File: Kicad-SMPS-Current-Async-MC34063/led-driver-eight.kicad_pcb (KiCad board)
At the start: 2 copper layers, 70 x 80 mm, 160 parts, among them J1 Input 12V-30V, J2 Output, J3 Conn_01x01, U1 MC34063, U2 LM321

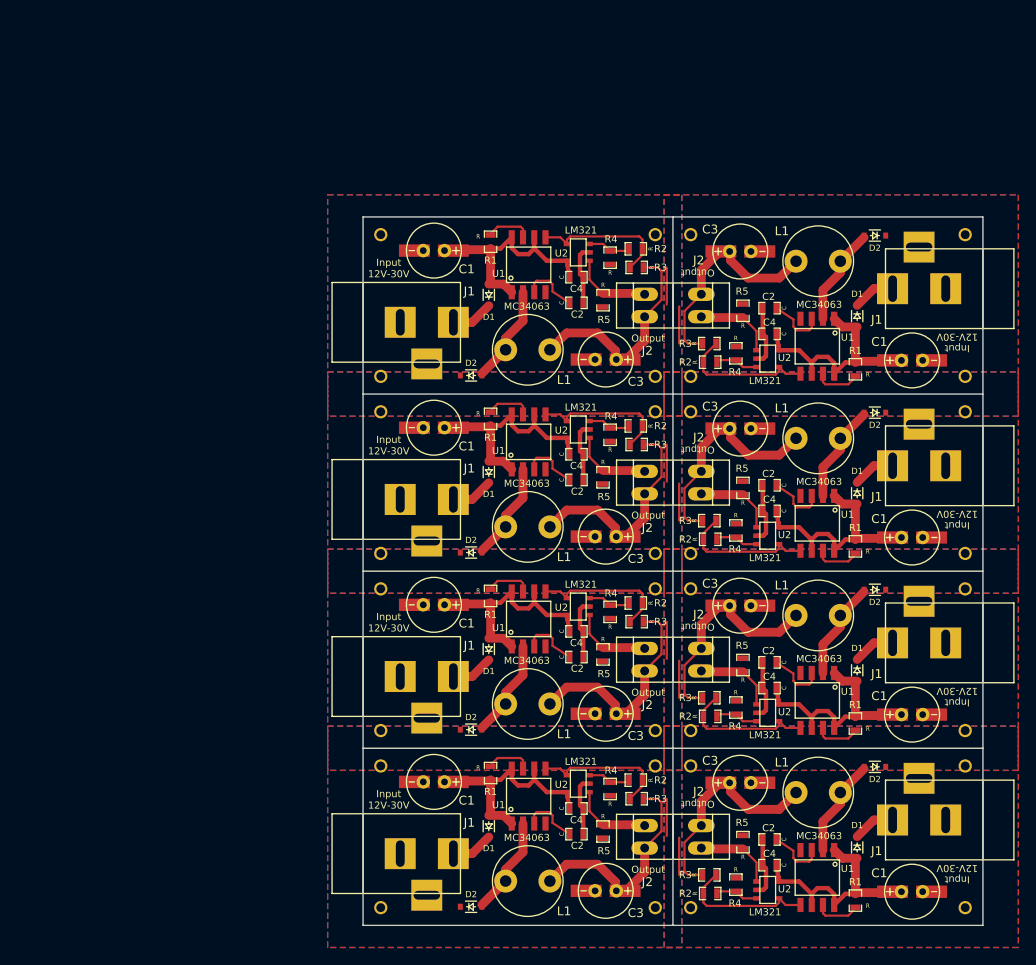
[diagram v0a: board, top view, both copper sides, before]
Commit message: Fix problem with current limiting resistor and also silk screen of diodes.
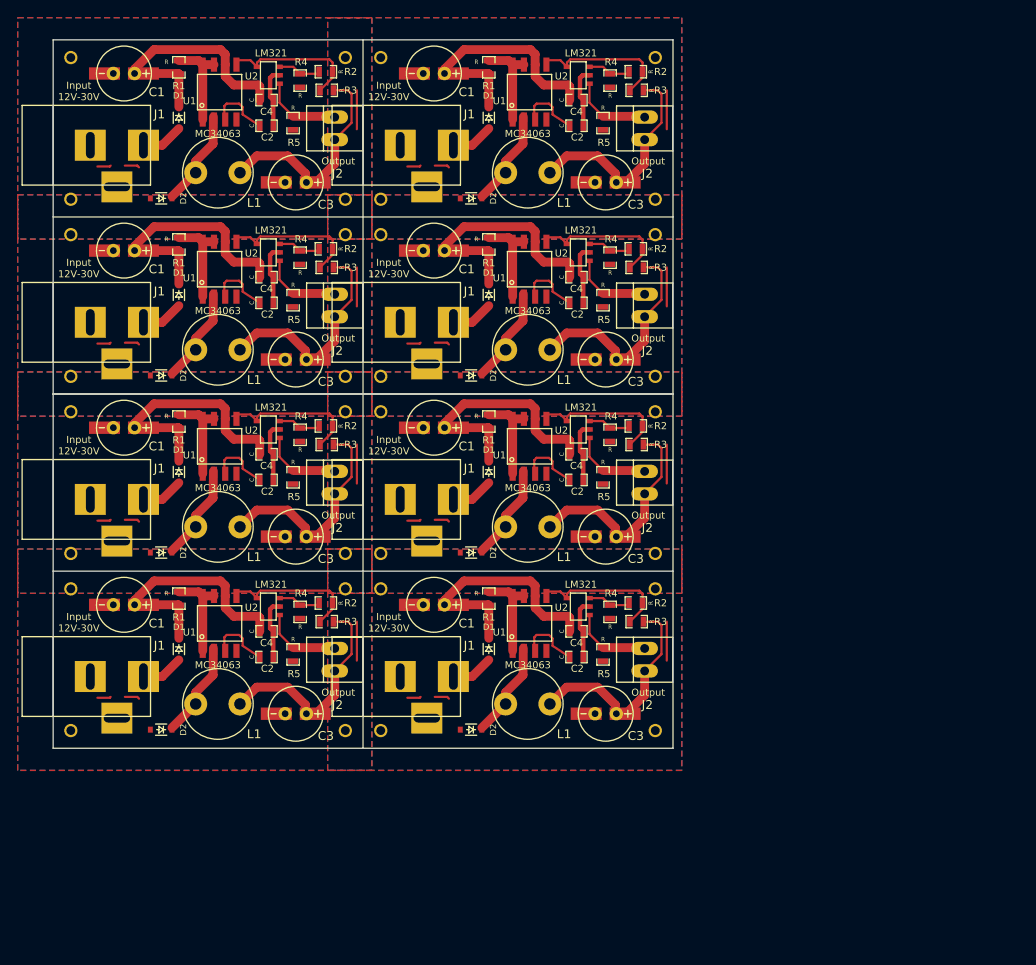
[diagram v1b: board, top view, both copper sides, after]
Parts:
- removed the C1 at (186.0, 83.7)
- removed the C1 at (186.0, 103.7)
- removed the C1 at (186.0, 143.7)
- removed the C1 at (186.0, 123.7)
- removed the C1 at (132.0, 131.3)
- removed the C2 at (169.9, 77.8)
- removed the C2 at (169.9, 97.8)
- removed the C2 at (169.9, 137.8)
- removed the C2 at (169.9, 117.8)
- removed the C2 at (148.1, 137.2)
- removed the C3 at (166.6, 71.4)
- removed the C3 at (166.6, 91.4)
- removed the C3 at (166.6, 131.4)
- removed the C3 at (166.6, 111.4)
- removed the C3 at (151.4, 143.6)
- removed the C4 at (169.9, 80.7)
- removed the C4 at (169.9, 100.7)
- removed the C4 at (169.9, 140.7)
- removed the C4 at (169.9, 120.7)
- removed the C4 at (148.1, 134.3)
- removed the D1 at (179.8, 78.7)
- removed the D1 at (179.8, 98.7)
- removed the D1 at (179.8, 138.7)
- removed the D1 at (179.8, 118.7)
- removed the D1 at (138.2, 136.3)
- removed the D2 at (181.8, 69.6)
- removed the D2 at (181.8, 89.6)
- removed the D2 at (181.8, 129.6)
- removed the D2 at (181.8, 109.6)
- removed the D2 at (136.2, 145.4)
- removed the J1 at (190.0, 75.6)
- removed the J1 at (190.0, 95.6)
- removed the J1 at (190.0, 135.6)
- removed the J1 at (190.0, 115.6)
- removed the J1 at (128.0, 139.4)
- removed the J2 at (162.2, 77.5)
- removed the J2 at (162.2, 97.5)
- removed the J2 at (162.2, 137.5)
- removed the J2 at (162.2, 117.5)
- removed the J2 at (155.8, 137.5)
- removed the J3 at (161.0, 85.5)
- removed the J3 at (192.0, 145.5)
- removed the J3 at (192.0, 129.5)
- removed the J3 at (161.0, 129.5)
- removed the J3 at (161.0, 109.5)
- removed the J3 at (192.0, 109.5)
- removed the J3 at (192.0, 125.5)
- removed the J3 at (161.0, 125.5)
- removed the J3 at (192.0, 85.5)
- removed the J3 at (157.0, 145.5)
- removed the J3 at (192.0, 69.5)
- removed the J3 at (126.0, 145.5)
- removed the J3 at (126.0, 129.5)
- removed the J3 at (157.0, 129.5)
- removed the J3 at (161.0, 69.5)
- removed the J3 at (161.0, 89.5)
- removed the J3 at (192.0, 89.5)
- removed the J3 at (192.0, 105.5)
- removed the J3 at (161.0, 105.5)
- removed the J3 at (161.0, 145.5)
- removed the L1 at (177.9, 72.5)
- removed the L1 at (177.9, 92.5)
- removed the L1 at (177.9, 132.5)
- removed the L1 at (177.9, 112.5)
- removed the L1 at (140.1, 142.5)
- removed the R1 at (179.6, 84.7)
- removed the R1 at (179.6, 104.7)
- removed the R1 at (179.6, 144.7)
- removed the R1 at (179.6, 124.7)
- removed the R1 at (138.4, 90.3)
- removed the R1 at (138.4, 70.3)
- removed the R1 at (138.4, 130.3)
- removed the R2 at (163.2, 83.9)
- removed the R2 at (163.2, 103.9)
- removed the R2 at (163.2, 143.9)
- removed the R2 at (163.2, 123.9)
- removed the R2 at (154.8, 131.1)
- removed the R3 at (163.1, 81.8)
- removed the R3 at (163.1, 101.8)
- removed the R3 at (163.1, 141.8)
- removed the R3 at (163.1, 121.8)
- removed the R3 at (154.9, 133.2)
- removed the R4 at (166.1, 82.9)
- removed the R4 at (166.1, 102.9)
- removed the R4 at (166.1, 142.9)
- removed the R4 at (166.1, 122.9)
- removed the R4 at (151.9, 132.1)
- removed the R5 at (166.9, 78.1)
- removed the R5 at (166.9, 98.1)
- removed the R5 at (166.9, 138.1)
- removed the R5 at (166.9, 118.1)
- removed the R5 at (151.1, 136.9)
- removed the U1 at (175.3, 82.1)
- removed the U1 at (175.3, 102.1)
- removed the U1 at (175.3, 142.1)
- removed the U1 at (175.3, 122.1)
- removed the U1 at (142.7, 92.9)
- removed the U1 at (142.7, 72.9)
- removed the U1 at (142.7, 132.9)
- removed the U2 at (169.7, 83.5)
- removed the U2 at (169.7, 103.5)
- removed the U2 at (169.7, 143.5)
- removed the U2 at (169.7, 123.5)
- removed the U2 at (148.3, 131.5)
- added C1: CP, smps-current-source:RADIAL_TABBED_2.5mm_6.3mm, F.Cu at (132.0, 51.3)
- added C1: CP, smps-current-source:RADIAL_TABBED_2.5mm_6.3mm, F.Cu at (97.0, 51.3)
- added C1: CP, smps-current-source:RADIAL_TABBED_2.5mm_6.3mm, F.Cu at (97.0, 71.3)
- added C1: CP, smps-current-source:RADIAL_TABBED_2.5mm_6.3mm, F.Cu at (97.0, 111.3)
- added C1: CP, smps-current-source:RADIAL_TABBED_2.5mm_6.3mm, F.Cu at (97.0, 91.3)
- added C2: C, smps-current-source:SM0603_Capa, F.Cu at (148.1, 57.2)
- added C2: C, smps-current-source:SM0603_Capa, F.Cu at (113.1, 57.2)
- added C2: C, smps-current-source:SM0603_Capa, F.Cu at (113.1, 77.2)
- added C2: C, smps-current-source:SM0603_Capa, F.Cu at (113.1, 117.2)
- added C2: C, smps-current-source:SM0603_Capa, F.Cu at (113.1, 97.2)
- added C3: CP, smps-current-source:RADIAL_TABBED_2.5mm_6.3mm, F.Cu at (151.4, 63.6)
- added C3: CP, smps-current-source:RADIAL_TABBED_2.5mm_6.3mm, F.Cu at (116.4, 63.6)
- added C3: CP, smps-current-source:RADIAL_TABBED_2.5mm_6.3mm, F.Cu at (116.4, 83.6)
- added C3: CP, smps-current-source:RADIAL_TABBED_2.5mm_6.3mm, F.Cu at (116.4, 123.6)
- added C3: CP, smps-current-source:RADIAL_TABBED_2.5mm_6.3mm, F.Cu at (116.4, 103.6)
- added C4: C, smps-current-source:SM0603_Capa, F.Cu at (148.1, 54.3)
- added C4: C, smps-current-source:SM0603_Capa, F.Cu at (113.1, 54.3)
- added C4: C, smps-current-source:SM0603_Capa, F.Cu at (113.1, 74.3)
- added C4: C, smps-current-source:SM0603_Capa, F.Cu at (113.1, 114.3)
- added C4: C, smps-current-source:SM0603_Capa, F.Cu at (113.1, 94.3)
- added D1: CUS15S30, smps-current-source:SOD-323, F.Cu at (138.2, 56.3)
- added D1: CUS15S30, smps-current-source:SOD-323, F.Cu at (103.2, 56.3)
- added D1: CUS15S30, smps-current-source:SOD-323, F.Cu at (103.2, 76.3)
- added D1: CUS15S30, smps-current-source:SOD-323, F.Cu at (103.2, 116.3)
- added D1: CUS15S30, smps-current-source:SOD-323, F.Cu at (103.2, 96.3)
- added D2: CUS15S30, smps-current-source:SOD-323, F.Cu at (136.2, 65.4)
- added D2: CUS15S30, smps-current-source:SOD-323, F.Cu at (101.2, 65.4)
- added D2: CUS15S30, smps-current-source:SOD-323, F.Cu at (101.2, 85.4)
- added D2: CUS15S30, smps-current-source:SOD-323, F.Cu at (101.2, 125.4)
- added D2: CUS15S30, smps-current-source:SOD-323, F.Cu at (101.2, 105.4)
- added J1: Input 12V-30V, smps-current-source:BARREL_JACK, F.Cu at (128.0, 59.4)
- added J1: Input 12V-30V, smps-current-source:BARREL_JACK, F.Cu at (93.0, 59.4)
- added J1: Input 12V-30V, smps-current-source:BARREL_JACK, F.Cu at (93.0, 79.4)
- added J1: Input 12V-30V, smps-current-source:BARREL_JACK, F.Cu at (93.0, 119.4)
- added J1: Input 12V-30V, smps-current-source:BARREL_JACK, F.Cu at (93.0, 99.4)
- added J2: Output, smps-current-source:PINHEAD1-2, F.Cu at (155.8, 57.5)
- added J2: Output, smps-current-source:PINHEAD1-2, F.Cu at (120.8, 57.5)
- added J2: Output, smps-current-source:PINHEAD1-2, F.Cu at (120.8, 77.5)
- added J2: Output, smps-current-source:PINHEAD1-2, F.Cu at (120.8, 117.5)
- added J2: Output, smps-current-source:PINHEAD1-2, F.Cu at (120.8, 97.5)
- added J3: Conn_01x01, smps-current-source:THROUGHVIA, F.Cu at (91.0, 65.5)
- added J3: Conn_01x01, smps-current-source:THROUGHVIA, F.Cu at (91.0, 49.5)
- added J3: Conn_01x01, smps-current-source:THROUGHVIA, F.Cu at (122.0, 49.5)
- added J3: Conn_01x01, smps-current-source:THROUGHVIA, F.Cu at (122.0, 69.5)
- added J3: Conn_01x01, smps-current-source:THROUGHVIA, F.Cu at (91.0, 69.5)
- added J3: Conn_01x01, smps-current-source:THROUGHVIA, F.Cu at (91.0, 85.5)
- added J3: Conn_01x01, smps-current-source:THROUGHVIA, F.Cu at (122.0, 85.5)
- added J3: Conn_01x01, smps-current-source:THROUGHVIA, F.Cu at (122.0, 125.5)
- added J3: Conn_01x01, smps-current-source:THROUGHVIA, F.Cu at (91.0, 125.5)
- added J3: Conn_01x01, smps-current-source:THROUGHVIA, F.Cu at (91.0, 109.5)
- added J3: Conn_01x01, smps-current-source:THROUGHVIA, F.Cu at (122.0, 109.5)
- added J3: Conn_01x01, smps-current-source:THROUGHVIA, F.Cu at (122.0, 89.5)
- added J3: Conn_01x01, smps-current-source:THROUGHVIA, F.Cu at (91.0, 89.5)
- added J3: Conn_01x01, smps-current-source:THROUGHVIA, F.Cu at (91.0, 105.5)
- added J3: Conn_01x01, smps-current-source:THROUGHVIA, F.Cu at (122.0, 105.5)
- added J3: Conn_01x01, smps-current-source:THROUGHVIA, F.Cu at (157.0, 49.5)
- added J3: Conn_01x01, smps-current-source:THROUGHVIA, F.Cu at (126.0, 49.5)
- added J3: Conn_01x01, smps-current-source:THROUGHVIA, F.Cu at (126.0, 65.5)
- added J3: Conn_01x01, smps-current-source:THROUGHVIA, F.Cu at (157.0, 65.5)
- added J3: Conn_01x01, smps-current-source:THROUGHVIA, F.Cu at (122.0, 65.5)
- added L1: L, smps-current-source:L_Radial_D7.8mm_P5.00mm_Fastron_07HCP, F.Cu at (140.1, 62.5)
- added L1: L, smps-current-source:L_Radial_D7.8mm_P5.00mm_Fastron_07HCP, F.Cu at (105.1, 62.5)
- added L1: L, smps-current-source:L_Radial_D7.8mm_P5.00mm_Fastron_07HCP, F.Cu at (105.1, 82.5)
- added L1: L, smps-current-source:L_Radial_D7.8mm_P5.00mm_Fastron_07HCP, F.Cu at (105.1, 122.5)
- added L1: L, smps-current-source:L_Radial_D7.8mm_P5.00mm_Fastron_07HCP, F.Cu at (105.1, 102.5)
- added R1: R, smps-current-source:SM0603_Resistor, F.Cu at (138.2, 70.6)
- added R1: R, smps-current-source:SM0603_Resistor, F.Cu at (138.2, 50.6)
- added R1: R, smps-current-source:SM0603_Resistor, F.Cu at (103.2, 50.6)
- added R1: R, smps-current-source:SM0603_Resistor, F.Cu at (103.2, 70.6)
- added R1: R, smps-current-source:SM0603_Resistor, F.Cu at (103.2, 110.6)
- added R1: R, smps-current-source:SM0603_Resistor, F.Cu at (103.2, 90.6)
- added R1: R, smps-current-source:SM0603_Resistor, F.Cu at (138.2, 90.6)
- added R2: R, smps-current-source:SM0603_Resistor, F.Cu at (154.8, 51.1)
- added R2: R, smps-current-source:SM0603_Resistor, F.Cu at (119.8, 51.1)
- added R2: R, smps-current-source:SM0603_Resistor, F.Cu at (119.8, 71.1)
- added R2: R, smps-current-source:SM0603_Resistor, F.Cu at (119.8, 111.1)
- added R2: R, smps-current-source:SM0603_Resistor, F.Cu at (119.8, 91.1)
- added R3: R, smps-current-source:SM0603_Resistor, F.Cu at (154.9, 53.2)
- added R3: R, smps-current-source:SM0603_Resistor, F.Cu at (119.9, 53.2)
- added R3: R, smps-current-source:SM0603_Resistor, F.Cu at (119.9, 73.2)
- added R3: R, smps-current-source:SM0603_Resistor, F.Cu at (119.9, 113.2)
- added R3: R, smps-current-source:SM0603_Resistor, F.Cu at (119.9, 93.2)
- added R4: R, smps-current-source:SM0603_Resistor, F.Cu at (151.9, 52.1)
- added R4: R, smps-current-source:SM0603_Resistor, F.Cu at (116.9, 52.1)
- added R4: R, smps-current-source:SM0603_Resistor, F.Cu at (116.9, 72.1)
- added R4: R, smps-current-source:SM0603_Resistor, F.Cu at (116.9, 112.1)
- added R4: R, smps-current-source:SM0603_Resistor, F.Cu at (116.9, 92.1)
- added R5: R, smps-current-source:SM0603_Resistor, F.Cu at (151.1, 56.9)
- added R5: R, smps-current-source:SM0603_Resistor, F.Cu at (116.1, 56.9)
- added R5: R, smps-current-source:SM0603_Resistor, F.Cu at (116.1, 76.9)
- added R5: R, smps-current-source:SM0603_Resistor, F.Cu at (116.1, 116.9)
- added R5: R, smps-current-source:SM0603_Resistor, F.Cu at (116.1, 96.9)
- added U1: MC34063, smps-current-source:SOIC_08_4.0mm_5.0mm_1.27mm, F.Cu at (142.8, 73.4)
- added U1: MC34063, smps-current-source:SOIC_08_4.0mm_5.0mm_1.27mm, F.Cu at (142.8, 53.4)
- added U1: MC34063, smps-current-source:SOIC_08_4.0mm_5.0mm_1.27mm, F.Cu at (107.8, 53.4)
- added U1: MC34063, smps-current-source:SOIC_08_4.0mm_5.0mm_1.27mm, F.Cu at (107.8, 73.4)
- added U1: MC34063, smps-current-source:SOIC_08_4.0mm_5.0mm_1.27mm, F.Cu at (107.8, 113.4)
- added U1: MC34063, smps-current-source:SOIC_08_4.0mm_5.0mm_1.27mm, F.Cu at (107.8, 93.4)
- added U1: MC34063, smps-current-source:SOIC_08_4.0mm_5.0mm_1.27mm, F.Cu at (142.8, 93.4)
- added U2: LM321, smps-current-source:SOT23-5, F.Cu at (148.3, 51.5)
- added U2: LM321, smps-current-source:SOT23-5, F.Cu at (113.3, 51.5)
- added U2: LM321, smps-current-source:SOT23-5, F.Cu at (113.3, 71.5)
- added U2: LM321, smps-current-source:SOT23-5, F.Cu at (113.3, 111.5)
- added U2: LM321, smps-current-source:SOT23-5, F.Cu at (113.3, 91.5)
- moved U1 0.51 mm to (142.8, 113.4)
- moved R1 0.36 mm to (138.2, 110.6)
- turned D1 to 90 degrees (x3)
- turned D2 to 0 degrees (x3)
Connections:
- U1 pad 1: /Vcc -> Net-(R1-Pad1)
- U1 pad 8: /Vcc -> Net-(R1-Pad1)
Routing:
- net Net-(R1-Pad1): track 41.4 -> 82.9 mm
- net (no net): track 33.6 -> 61.0 mm
- net /Vcc: track 216.4 -> 232.2 mm
- net Net-(D2-Pad1): track 90.6 -> 89.0 mm
